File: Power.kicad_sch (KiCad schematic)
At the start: 26 parts, among them J22 Conn_01x02_Socket, J23 Conn_01x02_Socket, J24 Conn_01x02_Socket, U10 INA219AxD, U15 TPS60400DBV, U9 INA219AxD

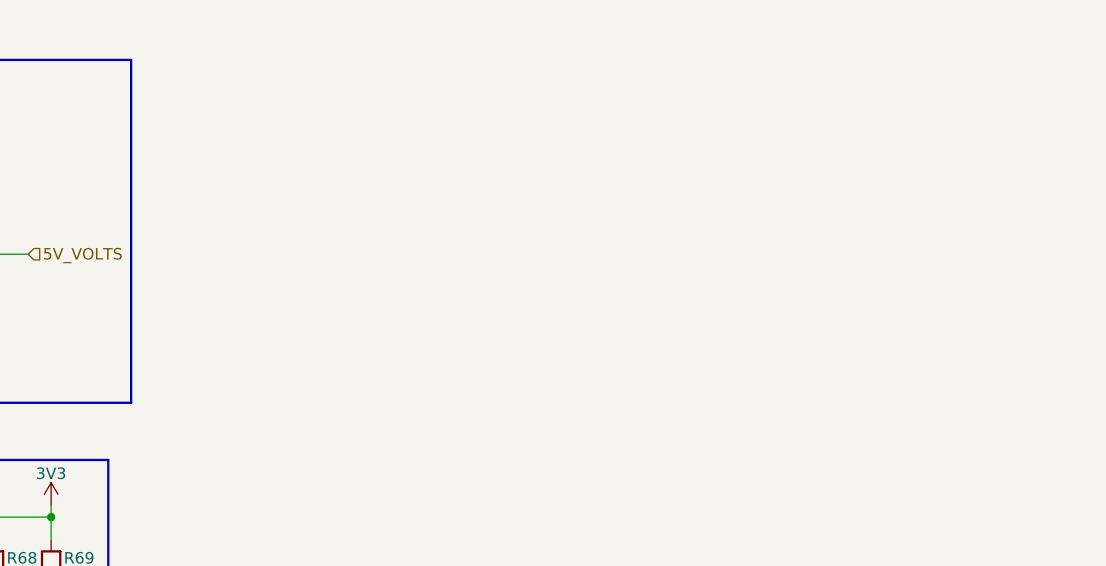
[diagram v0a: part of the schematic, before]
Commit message: got rid of pins on stm32
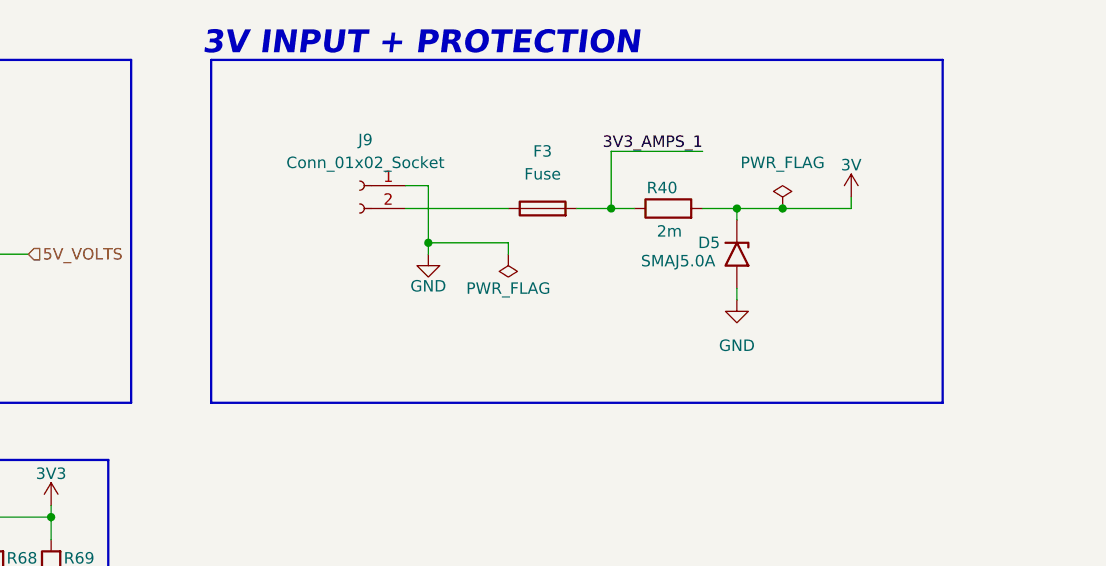
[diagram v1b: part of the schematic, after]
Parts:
- added D5: SMAJ5.0A, Diode_SMD:D_SMA, symbol Diode:SMAJ5.0A
- added F3: Fuse, Fuse:Fuse_1206_3216Metric, symbol Device:Fuse
- added J9: Conn_01x02_Socket, Connector_Phoenix_SPT:PhoenixContact_SPT_2.5_2-V-5.0-EX_1x02_P5.0mm_Vertical, symbol Connector:Conn_01x02_Socket
- added R40: 2m, Resistor_SMD:R_1206_3216Metric, symbol Device:R
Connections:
- net 3V3_AMPS_1: now also F3.2, R40.1
- net GND: now also D5.2 (A2), J9.1 (Pin_1)
- new net: F3.1, J9.2 (Pin_2)
- new net 3V: D5.1 (A1), R40.2
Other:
- note added: "3V INPUT + PROTECTION"
